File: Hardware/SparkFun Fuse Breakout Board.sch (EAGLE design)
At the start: 11 parts, among them J3 POWER_JACKPTH_LOCK

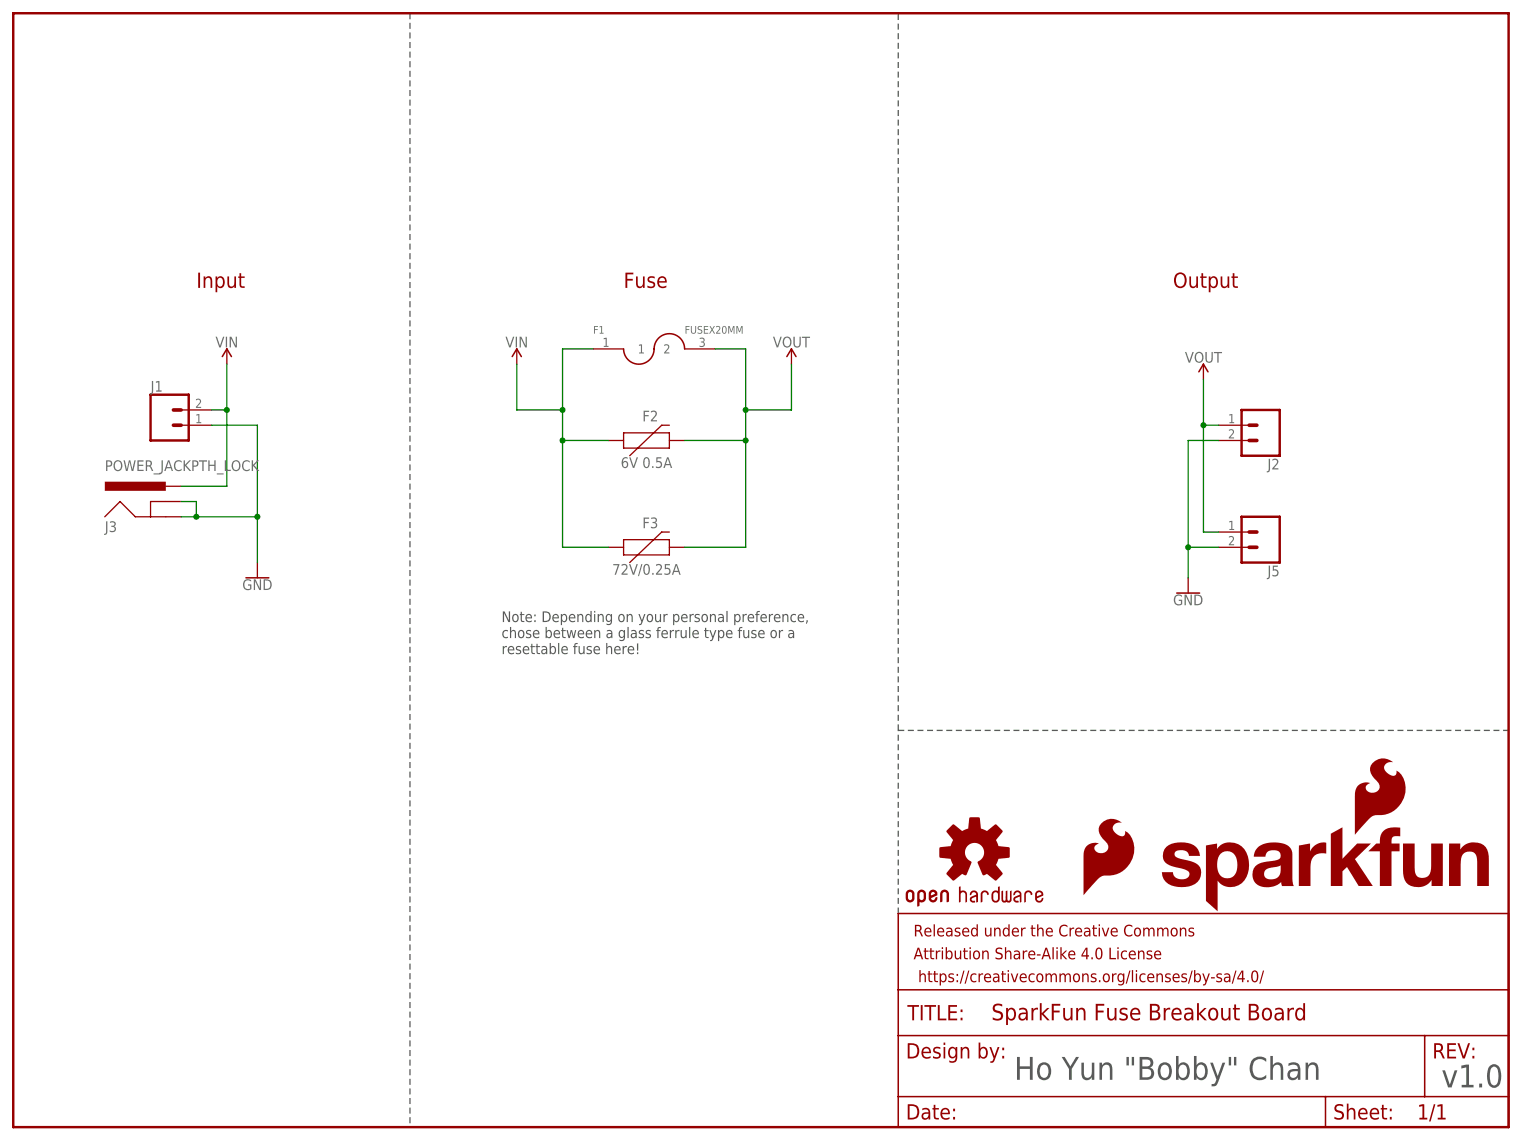
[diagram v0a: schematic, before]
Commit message: Update board
- rotate version number
- split top polygon layer to VIN and VOUT
- add t-stop isolate with screw terminals
- remove SMD Fuse
- remove 0.1" PTH pins
- use screw terminal instead of PTH pins
- adjust board size to accomodate screw terminals
- +/- label behind screw terminal output
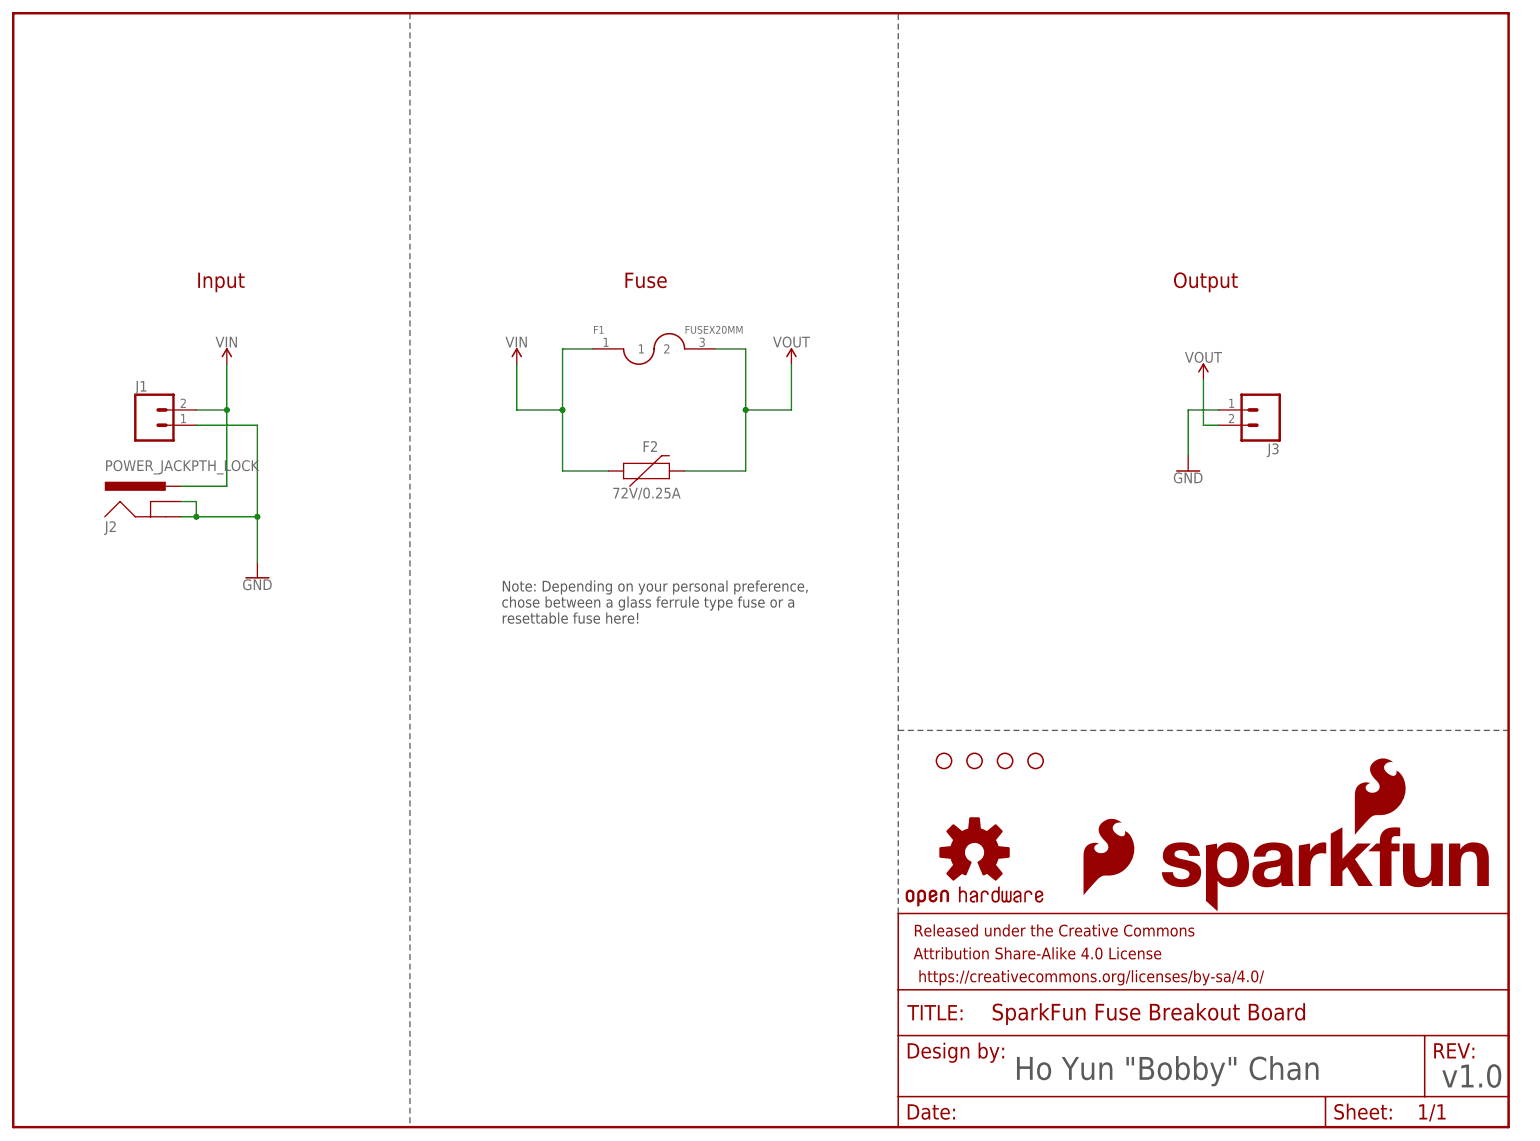
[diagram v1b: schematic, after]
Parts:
- removed F3: 72V/0.25A, SparkFun-Fuses:PPTC_PTH
- removed J5: (no value), SparkFun-Connectors:CONN_025MM
- added H1, H2, H3, H4: STAND-OFF, SparkFun-Hardware:STAND-OFF
- F2: value 6V 0.5A -> 72V/0.25A; device SparkFun-Fuses:PPTC_6V500MA -> SparkFun-Fuses:PPTC_PTH
- J1: device SparkFun-Connectors:CONN_02 -> SparkFun-Connectors:CONN_025MM
- J2: value (none) -> POWER_JACKPTH_LOCK; device SparkFun-Connectors:CONN_02 -> SparkFun-Connectors:POWER_JACKPTH_LOCK
- J3: value POWER_JACKPTH_LOCK -> (none); device SparkFun-Connectors:POWER_JACKPTH_LOCK -> SparkFun-Connectors:CONN_025MM
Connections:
- net GND: now also J2.GND, J2.GNDBREAK, J3.1; no longer J2.2, J3.GND, J3.GNDBREAK, J5.2
- net VIN: now also J2.PWR; no longer F3.1, J3.PWR
- net VOUT: now also J3.2; no longer F3.2, J2.1, J5.1
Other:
- moved on the sheet: F2, J1, J2, J3

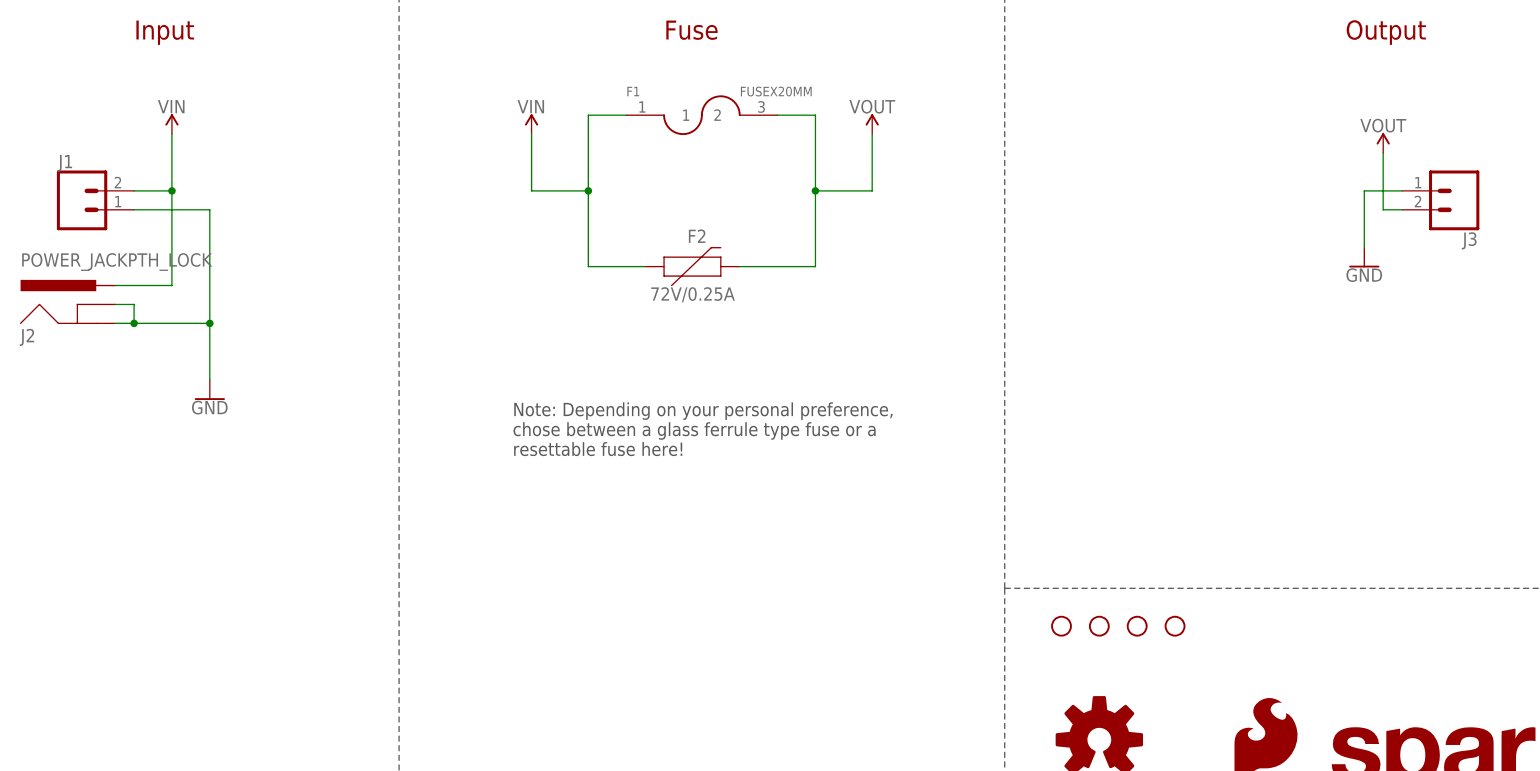
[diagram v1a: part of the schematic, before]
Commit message: Update Board
- move silkscreen for screw terminals
- remove stand offs and add top/bottom restrict for half mounting holes
- adjust isolation for polygon pours
- adjust polygon pour width for VIN and VOUT by F2
- big buzzard labels for VIN and VOUT
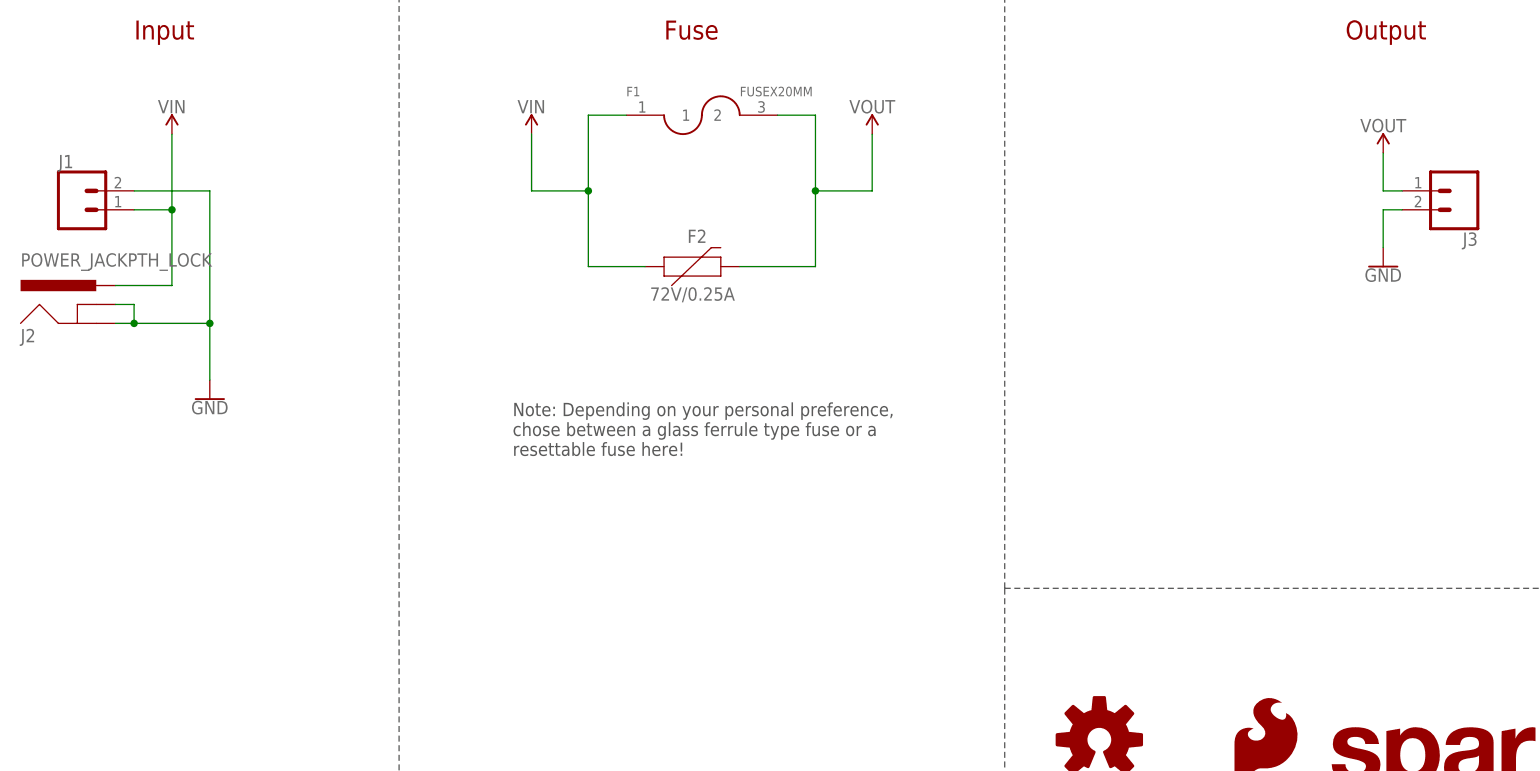
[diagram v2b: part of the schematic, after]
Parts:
- removed H1, H2, H3, H4: STAND-OFF, SparkFun-Hardware:STAND-OFF
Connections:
- net GND: now also J1.2, J3.2; no longer J1.1, J3.1
- net VIN: now also J1.1; no longer J1.2
- net VOUT: now also J3.1; no longer J3.2
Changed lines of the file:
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@@
 <part name="J1" library="SparkFun-Connectors" deviceset="CONN_02" device="5MM"/>
 <part name="J3" library="SparkFun-Connectors" deviceset="CONN_02" device="5MM"/>
-<part name="H1" library="SparkFun-Hardware" deviceset="STAND-OFF" device=""/>
-<part name="H2" library="SparkFun-Hardware" deviceset="STAND-OFF" device=""/>
-<part name="H3" library="SparkFun-Hardware" deviceset="STAND-OFF" device=""/>
-<part name="H4" library="SparkFun-Hardware" deviceset="STAND-OFF" device=""/>
 </parts>
 <sheets>
@@
 <instance part="GND1" gate="1" x="40.64" y="91.44"/>
 <instance part="F2" gate="F1" x="104.14" y="109.22"/>
-<instance part="GND3" gate="1" x="195.58" y="109.22"/>
+<instance part="GND3" gate="1" x="198.12" y="109.22"/>
 <instance part="SUPPLY2" gate="G$1" x="198.12" y="124.46"/>
 <instance part="SUPPLY1" gate="G$1" x="35.56" y="127"/>
@@
 <instance part="J1" gate="G$1" x="22.86" y="116.84"/>
 <instance part="J3" gate="G$1" x="208.28" y="119.38" rot="R180"/>
-<instance part="H1" gate="G$1" x="154.94" y="60.96"/>
-<instance part="H2" gate="G$1" x="160.02" y="60.96"/>
-<instance part="H3" gate="G$1" x="165.1" y="60.96"/>
-<instance part="H4" gate="G$1" x="170.18" y="60.96"/>
 </instances>
 <busses>
@@
 <pinref part="J2" gate="G$1" pin="PWR"/>
 <wire x1="27.94" y1="106.68" x2="35.56" y2="106.68" width="0.1524" layer="91"/>
-<wire x1="35.56" y1="106.68" x2="35.56" y2="119.38" width="0.1524" layer="91"/>
 <pinref part="SUPPLY1" gate="G$1" pin="VIN"/>
-<wire x1="35.56" y1="127" x2="35.56" y2="119.38" width="0.1524" layer="91"/>
-<junction x="35.56" y="119.38"/>
-<pinref part="J1" gate="G$1" pin="2"/>
-<wire x1="30.48" y1="119.38" x2="35.56" y2="119.38" width="0.1524" layer="91"/>
+<wire x1="35.56" y1="127" x2="35.56" y2="116.84" width="0.1524" layer="91"/>
+<pinref part="J1" gate="G$1" pin="1"/>
+<wire x1="35.56" y1="116.84" x2="35.56" y2="106.68" width="0.1524" layer="91"/>
+<wire x1="35.56" y1="116.84" x2="30.48" y2="116.84" width="0.1524" layer="91"/>
+<junction x="35.56" y="116.84"/>
 </segment>
 </net>
@@
 <wire x1="30.48" y1="104.14" x2="30.48" y2="101.6" width="0.1524" layer="91"/>
 <junction x="30.48" y="101.6"/>
-<wire x1="30.48" y1="116.84" x2="40.64" y2="116.84" width="0.1524" layer="91"/>
-<wire x1="40.64" y1="116.84" x2="40.64" y2="101.6" width="0.1524" layer="91"/>
+<wire x1="40.64" y1="119.38" x2="40.64" y2="101.6" width="0.1524" layer="91"/>
 <junction x="40.64" y="101.6"/>
-<pinref part="J1" gate="G$1" pin="1"/>
+<pinref part="J1" gate="G$1" pin="2"/>
+<wire x1="40.64" y1="119.38" x2="30.48" y2="119.38" width="0.1524" layer="91"/>
 </segment>
 <segment>
 <pinref part="GND3" gate="1" pin="GND"/>
-<wire x1="195.58" y1="119.38" x2="195.58" y2="111.76" width="0.1524" layer="91"/>
-<wire x1="200.66" y1="119.38" x2="195.58" y2="119.38" width="0.1524" layer="91"/>
-<pinref part="J3" gate="G$1" pin="1"/>
+<wire x1="198.12" y1="116.84" x2="198.12" y2="111.76" width="0.1524" layer="91"/>
+<pinref part="J3" gate="G$1" pin="2"/>
+<wire x1="200.66" y1="116.84" x2="198.12" y2="116.84" width="0.1524" layer="91"/>
 </segment>
 </net>
@@
 </segment>
 <segment>
-<wire x1="198.12" y1="116.84" x2="198.12" y2="124.46" width="0.1524" layer="91"/>
+<wire x1="198.12" y1="119.38" x2="198.12" y2="124.46" width="0.1524" layer="91"/>
 <pinref part="SUPPLY2" gate="G$1" pin="VOUT"/>
-<pinref part="J3" gate="G$1" pin="2"/>
-<wire x1="200.66" y1="116.84" x2="198.12" y2="116.84" width="0.1524" layer="91"/>
+<pinref part="J3" gate="G$1" pin="1"/>
+<wire x1="198.12" y1="119.38" x2="200.66" y2="119.38" width="0.1524" layer="91"/>
 </segment>
 </net>
